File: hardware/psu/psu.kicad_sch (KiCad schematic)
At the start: 57 parts, among them J1 Conn_01x02, J10 Conn_01x04, J11 Conn_01x03, J12 Conn_01x02, J13 Conn_01x03, J2 Conn_01x05, J3 Conn_01x02, J4 Conn_01x06, J5 Conn_01x03, J6 Conn_01x05, J7 Conn_01x08, J8 Conn_01x03, J9 Conn_01x04, SW1 SW_SPST, T1 AS-1T175, U1 LM7905_TO220

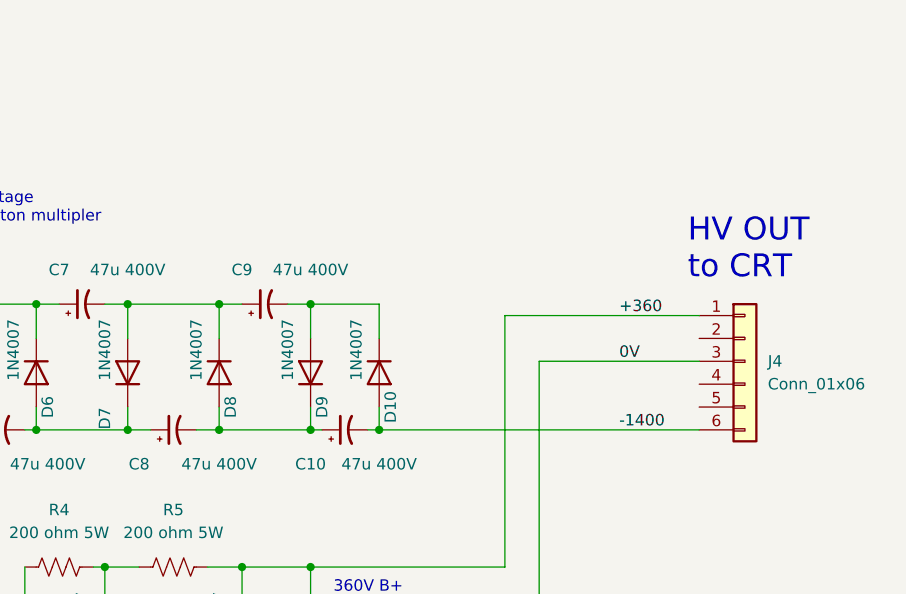
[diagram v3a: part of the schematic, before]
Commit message: Add CRT voltage select jumper
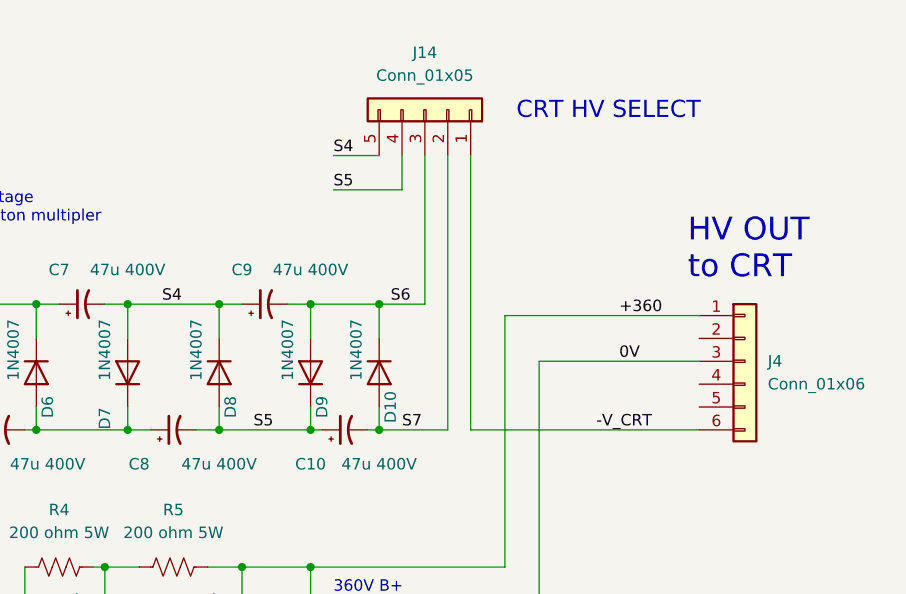
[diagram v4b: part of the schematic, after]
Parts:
- added J14: Conn_01x05, Connector_Molex:Molex_KK-396_5273-05A_1x05_P3.96mm_Vertical, symbol Connector_Generic:Conn_01x05
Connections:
- net S5: now reaches C10.1, C8.2, D8.2 (A), D9.1 (K)
- net S5: now also J14.4 (Pin_4)
- net S6: now reaches C9.2, D10.1 (K), D9.2 (A)
- net S6: now also J14.3 (Pin_3)
- net S4: now reaches C7.2, C9.1, D7.2 (A), D8.1 (K)
- net S4: now also J14.5 (Pin_5)
- net -1400 renamed S7
- net S7: now also J14.2 (Pin_2); no longer J4.6 (Pin_6)
- new net -V_CRT: J14.1 (Pin_1), J4.6 (Pin_6)
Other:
- note added: "CRT HV SELECT"
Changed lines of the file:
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@@
   (junction (at 186.69 93.98) (diameter 0) (color 0 0 0 0)
   )
+  (junction (at 194.31 59.69) (diameter 0) (color 0 0 0 0)
+  )
   (junction (at 106.68 134.62) (diameter 0) (color 0 0 0 0)
   )
   (junction (at 200.66 154.94) (diameter 0) (color 0 0 0 0)
   )
-  (junction (at 194.31 59.69) (diameter 0) (color 0 0 0 0)
-  )
   (junction (at 191.77 137.16) (diameter 0) (color 0 0 0 0)
   )
@@
   (junction (at 128.27 45.72) (diameter 0) (color 0 0 0 0)
   )
+  (junction (at 194.31 45.72) (diameter 0) (color 0 0 0 0)
+  )
   (junction (at 124.46 86.36) (diameter 0) (color 0 0 0 0)
   )
@@
     (stroke (width 0) (type default) (color 0 0 0 0))
   )
+  (wire (pts (xy 194.31 45.72) (xy 199.39 45.72))
+    (stroke (width 0) (type default) (color 0 0 0 0))
+  )
   (wire (pts (xy 105.41 137.16) (xy 105.41 161.29))
     (stroke (width 0) (type default) (color 0 0 0 0))
@@
     (stroke (width 0) (type default) (color 0 0 0 0))
   )
+  (wire (pts (xy 201.93 29.21) (xy 201.93 59.69))
+    (stroke (width 0) (type default) (color 0 0 0 0))
+  )
   (wire (pts (xy 149.86 107.95) (xy 175.26 107.95))
     (stroke (width 0) (type default) (color 0 0 0 0))
@@
     (stroke (width 0) (type default) (color 0 0 0 0))
   )
+  (wire (pts (xy 204.47 29.21) (xy 204.47 59.69))
+    (stroke (width 0) (type default) (color 0 0 0 0))
+  )
   (wire (pts (xy 232.41 123.19) (xy 232.41 137.16))
     (stroke (width 0) (type default) (color 0 0 0 0))
@@
     (stroke (width 0) (type default) (color 0 0 0 0))
   )
+  (wire (pts (xy 199.39 29.21) (xy 199.39 45.72))
+    (stroke (width 0) (type default) (color 0 0 0 0))
+  )
   (wire (pts (xy 60.96 171.45) (xy 69.85 171.45))
     (stroke (width 0) (type default) (color 0 0 0 0))
@@
     (stroke (width 0) (type default) (color 0 0 0 0))
   )
+  (wire (pts (xy 189.23 29.21) (xy 194.31 29.21))
+    (stroke (width 0) (type default) (color 0 0 0 0))
+  )
   (wire (pts (xy 149.86 128.27) (xy 157.48 128.27))
     (stroke (width 0) (type default) (color 0 0 0 0))
@@
     (stroke (width 0) (type default) (color 0 0 0 0))
   )
-  (wire (pts (xy 194.31 59.69) (xy 229.87 59.69))
-    (stroke (width 0) (type default) (color 0 0 0 0))
-  )
   (wire (pts (xy 137.16 73.66) (xy 134.62 73.66))
     (stroke (width 0) (type default) (color 0 0 0 0))
@@
     (stroke (width 0) (type default) (color 0 0 0 0))
   )
+  (wire (pts (xy 229.87 59.69) (xy 204.47 59.69))
+    (stroke (width 0) (type default) (color 0 0 0 0))
+  )
   (wire (pts (xy 109.22 124.46) (xy 106.68 124.46))
     (stroke (width 0) (type default) (color 0 0 0 0))
@@
     (stroke (width 0) (type default) (color 0 0 0 0))
   )
+  (wire (pts (xy 196.85 29.21) (xy 196.85 33.02))
+    (stroke (width 0) (type default) (color 0 0 0 0))
+  )
   (wire (pts (xy 106.68 134.62) (xy 106.68 124.46))
     (stroke (width 0) (type default) (color 0 0 0 0))
@@
     (stroke (width 0) (type default) (color 0 0 0 0))
   )
+  (wire (pts (xy 189.23 33.02) (xy 196.85 33.02))
+    (stroke (width 0) (type default) (color 0 0 0 0))
+  )
   (wire (pts (xy 74.93 76.2) (xy 71.12 76.2))
     (stroke (width 0) (type default) (color 0 0 0 0))
@@
   )
   (wire (pts (xy 29.21 173.99) (xy 39.37 173.99))
+    (stroke (width 0) (type default) (color 0 0 0 0))
+  )
+  (wire (pts (xy 194.31 59.69) (xy 201.93 59.69))
     (stroke (width 0) (type default) (color 0 0 0 0))
   )
@@
     (effects (font (size 1.905 1.905)) (justify left bottom))
   )
+  (text "CRT HV SELECT" (at 209.55 25.4 0)
+    (effects (font (size 1.905 1.905)) (justify left bottom))
+  )
   (text "+360, -1.4kV for CRT (2mA)\n+5, +3.3 for logic (1A)"
     (at 170.18 182.88 0)
@@
     (effects (font (size 1.27 1.27)) (justify left bottom))
   )
+  (label "S4" (at 189.23 29.21 0)
+    (effects (font (size 1.27 1.27)) (justify left bottom))
+  )
   (label "6.3_2B" (at 97.79 107.95 0)
     (effects (font (size 1.27 1.27)) (justify left bottom))
   )
+  (label "-V_CRT" (at 218.44 59.69 0)
+    (effects (font (size 1.27 1.27)) (justify left bottom))
+  )
   (label "SW_ACL" (at 93.98 121.92 0)
     (effects (font (size 1.27 1.27)) (justify left bottom))
@@
     (effects (font (size 1.27 1.27)) (justify left bottom))
   )
+  (label "S5" (at 180.34 59.69 0)
+    (effects (font (size 1.27 1.27)) (justify left bottom))
+  )
   (label "175_1A" (at 97.79 60.96 0)
     (effects (font (size 1.27 1.27)) (justify left bottom))
@@
     (effects (font (size 1.27 1.27)) (justify left bottom))
   )
+  (label "S4" (at 170.18 45.72 0)
+    (effects (font (size 1.27 1.27)) (justify left bottom))
+  )
   (label "ACN" (at 29.21 173.99 0)
     (effects (font (size 1.27 1.27)) (justify left bottom))
@@
     (effects (font (size 1.27 1.27)) (justify left bottom))
   )
-  (label "-1400" (at 220.98 59.69 0)
+  (label "S5" (at 189.23 33.02 0)
+    (effects (font (size 1.27 1.27)) (justify left bottom))
+  )
+  (label "S7" (at 196.85 59.69 0)
+    (effects (font (size 1.27 1.27)) (justify left bottom))
+  )
+  (label "S6" (at 195.58 45.72 0)
     (effects (font (size 1.27 1.27)) (justify left bottom))
   )
@@
     (pin "2")
   )
+  (symbol (lib_id "Connector_Generic:Conn_01x05") (at 199.39 24.13 270) (mirror x) (unit 1)
+    (in_bom yes) (on_board yes) (fields_autoplaced)
+    (property "Reference" "J14" (id 0) (at 199.39 17.78 90))
+    (property "Value" "Conn_01x05" (id 1) (at 199.39 20.32 90))
+    (property "Footprint" "Connector_Molex:Molex_KK-396_5273-05A_1x05_P3.96mm_Vertical" (id 2) (at 199.39 24.13 0)
+      (effects (font (size 1.27 1.27)) hide)
+    )
+    (property "Datasheet" "~" (id 3) (at 199.39 24.13 0)
+      (effects (font (size 1.27 1.27)) hide)
+    )
+    (pin "1")
+    (pin "2")
+    (pin "3")
+    (pin "4")
+    (pin "5")
+  )
   (symbol (lib_id "power:GND") (at 71.12 99.06 0) (unit 1)
     (in_bom yes) (on_board yes) (fields_autoplaced)
@@
   )
   (symbol (lib_id "Antek:AS-1T175") (at 85.09 71.12 0) (unit 1)
-    (in_bom yes) (on_board yes) (fields_autoplaced)
+    (in_bom yes) (on_board no) (fields_autoplaced)
     (property "Reference" "T1" (id 0) (at 85.09 53.34 0))
     (property "Value" "AS-1T175" (id 1) (at 85.09 55.88 0))
@@
       (reference "J13") (unit 1) (value "Conn_01x03") (footprint "Connector_Molex:Molex_KK-396_A-41791-0003_1x03_P3.96mm_Vertical")
     )
+    (path "/2ab95dea-521b-40e4-9f56-b9837163bbbd"
+      (reference "J14") (unit 1) (value "Conn_01x05") (footprint "Connector_Molex:Molex_KK-396_5273-05A_1x05_P3.96mm_Vertical")
+    )
     (path "/67bad454-12b9-4442-88f0-78770ce3ebda"
